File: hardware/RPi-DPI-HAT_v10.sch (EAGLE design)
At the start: 71 parts, among them IC1 LDO-TS9011-3V3, J20_1 JUMPER2-0402, J40_1 JUMPER2-0402, J40_2 JUMPER2-0402, X1 PASSER-07, X2 PASSER-07, X3 PASSER-07

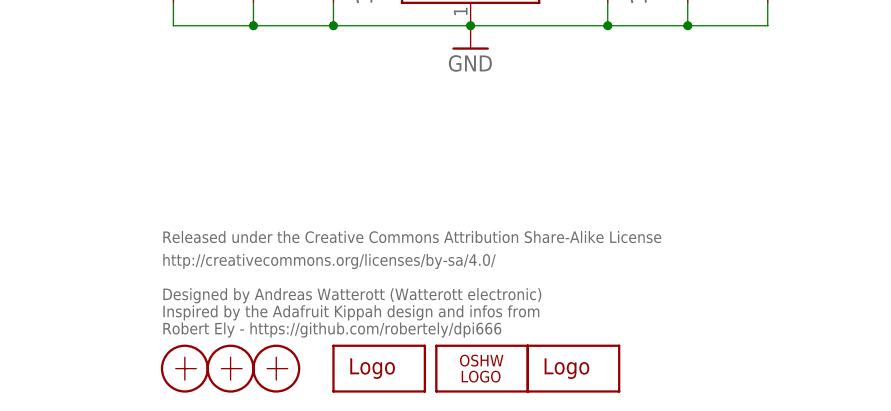
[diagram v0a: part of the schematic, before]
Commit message: updated schematics
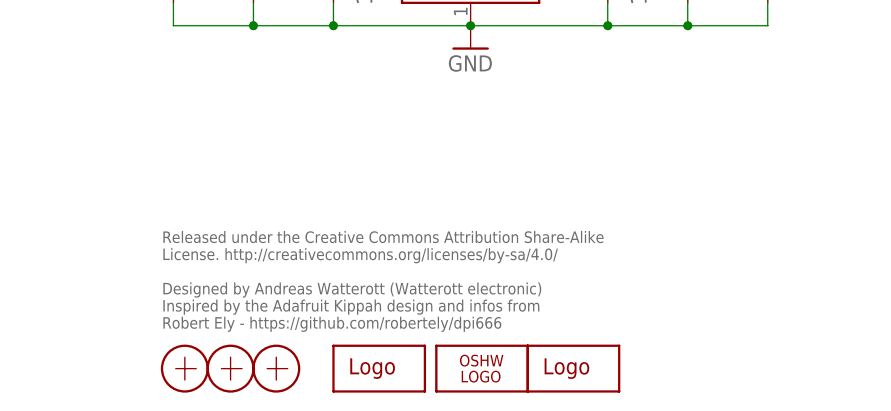
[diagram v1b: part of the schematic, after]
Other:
- note added: "Released under the Creative Commons Attribution Share-Alike License. http://creativecommons.org/licenses/by-sa/4.0/ Designed by Andreas Watterott (Watterott electronic) Inspired by the Adafruit Kippah design and infos from Robert Ely - https://github.com/robertely/dpi666"
- note removed: "Designed by Andreas Watterott (Watterott electronic)"
- note removed: "Inspired by the Adafruit Kippah design and infos from Robert Ely - https://github.com/robertely/dpi666"
- note removed: "Released under the Creative Commons Attribution Share-Alike License"
- note removed: "http://creativecommons.org/licenses/by-sa/4.0/"
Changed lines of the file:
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@@
 <?xml version="1.0" encoding="utf-8"?>
 <!DOCTYPE eagle SYSTEM "eagle.dtd">
-<eagle version="7.3.0">
+<eagle version="7.5.0">
 <drawing>
 <settings>
@@
 <setting verticaltext="up"/>
 </settings>
-<grid distance="0.1" unitdist="inch" unit="inch" style="lines" multiple="1" display="no" altdistance="0.01" altunitdist="inch" altunit="inch"/>
+<grid distance="0.05" unitdist="inch" unit="inch" style="lines" multiple="1" display="yes" altdistance="0.025" altunitdist="inch" altunit="inch"/>
 <layers>
 <layer number="1" name="Top" color="4" fill="1" visible="no" active="no"/>
@@
 <layer number="51" name="tDocu" color="7" fill="1" visible="no" active="no"/>
 <layer number="52" name="bDocu" color="7" fill="1" visible="no" active="no"/>
-<layer number="53" name="tCopper" color="7" fill="11" visible="no" active="no"/>
-<layer number="54" name="bCopper" color="7" fill="1" visible="no" active="no"/>
-<layer number="56" name="wert" color="7" fill="1" visible="no" active="no"/>
-<layer number="57" name="tCAD" color="7" fill="1" visible="no" active="no"/>
 <layer number="90" name="Modules" color="5" fill="1" visible="yes" active="yes"/>
 <layer number="91" name="Nets" color="2" fill="1" visible="yes" active="yes"/>
@@
 <layer number="98" name="Guide" color="6" fill="1" visible="yes" active="yes"/>
 <layer number="99" name="SpiceOrder" color="5" fill="1" visible="yes" active="yes"/>
-<layer number="100" name="Muster" color="7" fill="1" visible="no" active="no"/>
-<layer number="153" name="FabDoc1" color="6" fill="1" visible="no" active="no"/>
-<layer number="154" name="FabDoc2" color="2" fill="1" visible="no" active="no"/>
-<layer number="155" name="FabDoc3" color="7" fill="15" visible="no" active="no"/>
-<layer number="200" name="200bmp" color="1" fill="10" visible="no" active="no"/>
-<layer number="217" name="217bmp" color="18" fill="1" visible="no" active="no"/>
-<layer number="218" name="218bmp" color="19" fill="1" visible="no" active="no"/>
-<layer number="219" name="219bmp" color="20" fill="1" visible="no" active="no"/>
-<layer number="220" name="220bmp" color="21" fill="1" visible="no" active="no"/>
-<layer number="221" name="221bmp" color="22" fill="1" visible="no" active="no"/>
-<layer number="222" name="222bmp" color="23" fill="1" visible="no" active="no"/>
-<layer number="223" name="223bmp" color="24" fill="1" visible="no" active="no"/>
-<layer number="224" name="224bmp" color="25" fill="1" visible="no" active="no"/>
 <layer number="250" name="Descript" color="3" fill="1" visible="yes" active="yes"/>
-<layer number="251" name="SMDround" color="12" fill="11" visible="no" active="no"/>
 </layers>
 <schematic xreflabel="%F%N/%S.%C%R" xrefpart="/%S.%C%R">
@@
 <plain>
 <text x="180.34" y="152.4" size="3.81" layer="250">Raspberry Pi</text>
-<text x="162.56" y="21.59" size="1.27" layer="95">Released under the Creative Commons Attribution Share-Alike License</text>
-<text x="162.56" y="19.05" size="1.27" layer="95">http://creativecommons.org/licenses/by-sa/4.0/</text>
-<text x="162.56" y="15.24" size="1.27" layer="95">Designed by Andreas Watterott (Watterott electronic)</text>
+<text x="162.56" y="22.86" size="1.27" layer="95" align="top-left">Released under the Creative Commons Attribution Share-Alike
+License. http://creativecommons.org/licenses/by-sa/4.0/
+Designed by Andreas Watterott (Watterott electronic)
+Inspired by the Adafruit Kippah design and infos from
+Robert Ely - https://github.com/robertely/dpi666</text>
 <text x="118.11" y="38.1" size="1.778" layer="96" rot="R90">I = 0.3V / RS</text>
 <text x="59.69" y="52.705" size="1.27" layer="96" align="center">Digikey 490-5340-6-ND</text>
@@
 <wire x1="118.11" y1="127" x2="120.65" y2="127" width="0.4064" layer="94"/>
 <text x="63.5" y="163.83" size="3.81" layer="250">TFT Display</text>
-<text x="162.56" y="11.43" size="1.27" layer="95">Inspired by the Adafruit Kippah design and infos from
-Robert Ely - https://github.com/robertely/dpi666</text>
 </plain>
 <instances>
